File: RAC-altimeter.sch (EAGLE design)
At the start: 16 parts, among them IC1 BMI088, IC2 BMP388, IC3 STM32L412KBU6, J1 MICRO-SD

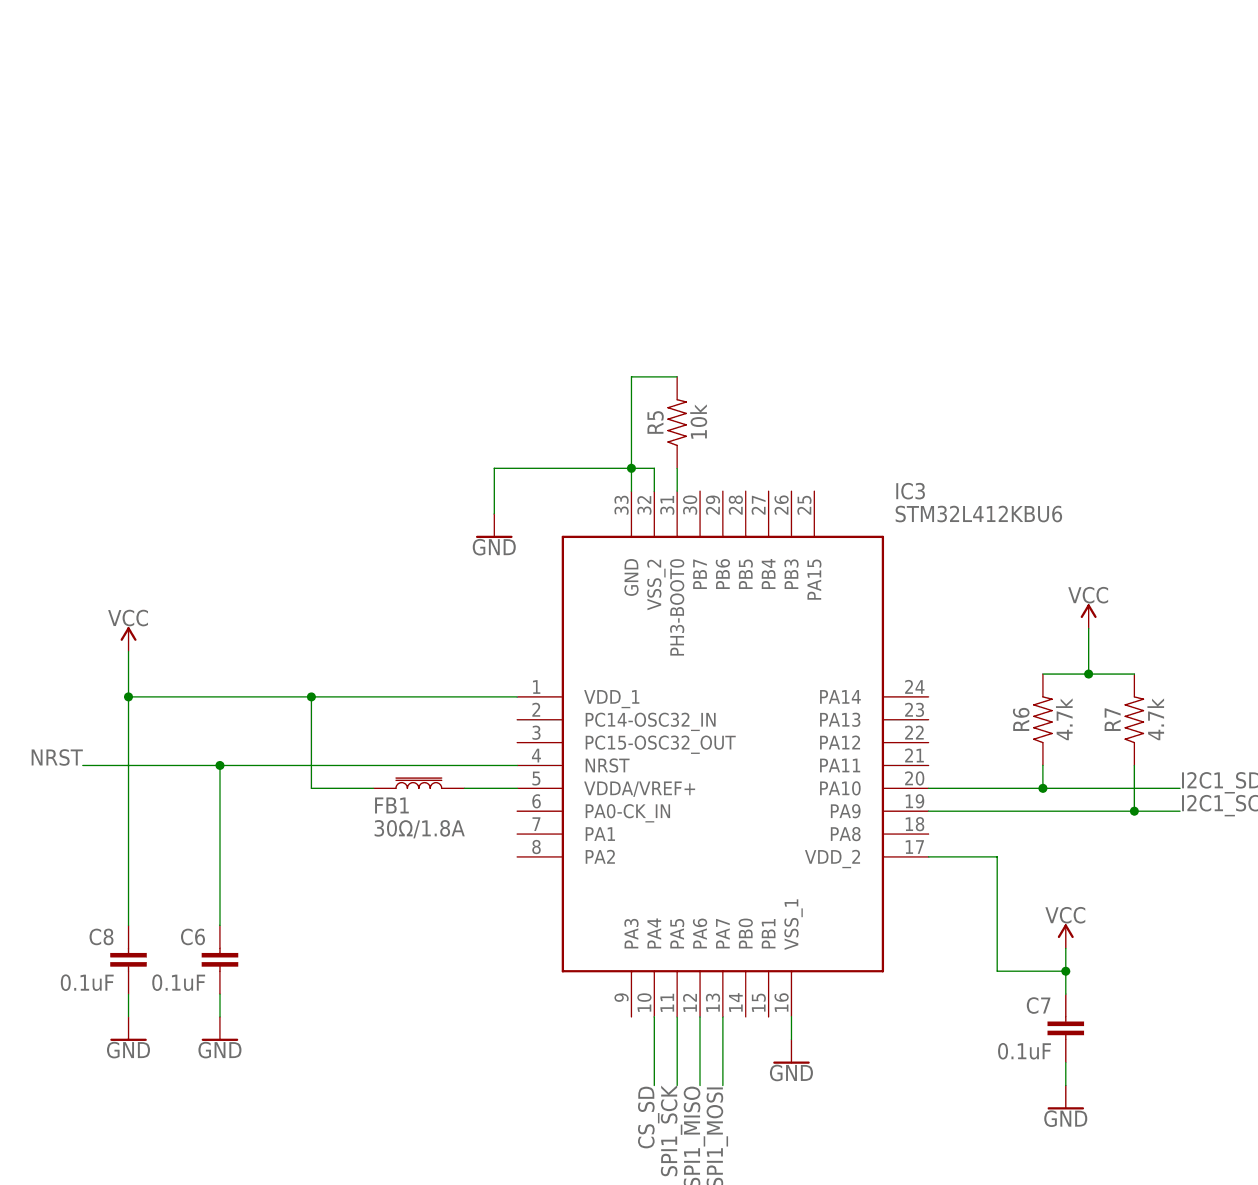
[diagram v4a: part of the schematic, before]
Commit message: Connected the TPS73733 LDO
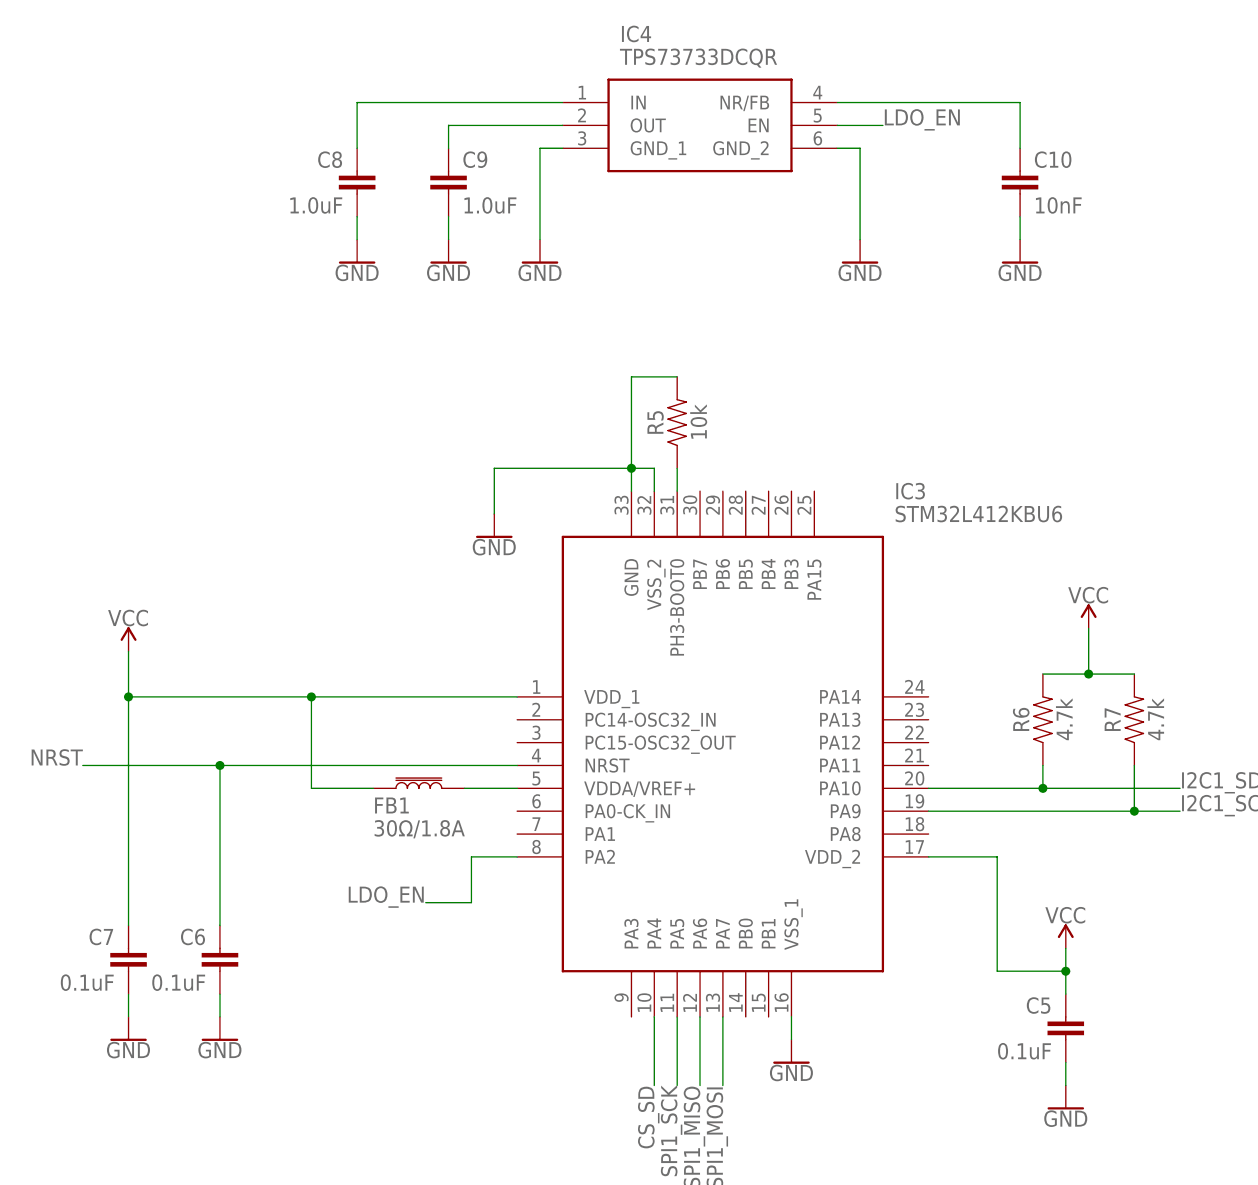
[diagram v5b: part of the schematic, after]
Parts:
- added C10: 10nF, SparkFun-Capacitors:10NF-0603-50V-10%
- added C5: 0.1uF, SparkFun-Capacitors:0.1UF-0603-25V-(+80/-20%)
- added C9: 1.0uF, SparkFun-Capacitors:1.0UF-0603-16V-10%
- added IC4: TPS73733DCQR, RAC-Altimeter:TPS73733DCQR
- C8: value 0.1uF -> 1.0uF; device SparkFun-Capacitors:0.1UF-0603-25V-(+80/-20%) -> SparkFun-Capacitors:1.0UF-0603-16V-10%
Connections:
- new net LDO_EN: IC3.PA2, IC4.EN
- new net N$1: C8.1, IC4.IN
- new net N$2: C9.1, IC4.OUT
- new net N$8: C10.1, IC4.NR/FB
- net GND: now also C10.2, C5.2, C9.2, IC4.GND_1, IC4.GND_2
- net VCC: now also C5.1; no longer C8.1
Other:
- moved on the sheet: C7, C8
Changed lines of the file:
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@@
 <?xml version="1.0" encoding="utf-8"?>
 <!DOCTYPE eagle SYSTEM "eagle.dtd">
-<eagle version="9.4.1">
+<eagle version="9.4.2">
 <drawing>
 <settings>
@@
 <part name="C6" library="SparkFun-Capacitors" deviceset="0.1UF" device="-0603-25V-(+80/-20%)" value="0.1uF"/>
 <part name="GND7" library="SparkFun-PowerSymbols" library_urn="urn:adsk.eagle:library:530" deviceset="GND" device=""/>
+<part name="C5" library="SparkFun-Capacitors" deviceset="0.1UF" device="-0603-25V-(+80/-20%)" value="0.1uF"/>
+<part name="GND8" library="SparkFun-PowerSymbols" library_urn="urn:adsk.eagle:library:530" deviceset="GND" device=""/>
 <part name="C7" library="SparkFun-Capacitors" deviceset="0.1UF" device="-0603-25V-(+80/-20%)" value="0.1uF"/>
-<part name="GND8" library="SparkFun-PowerSymbols" library_urn="urn:adsk.eagle:library:530" deviceset="GND" device=""/>
-<part name="C8" library="SparkFun-Capacitors" deviceset="0.1UF" device="-0603-25V-(+80/-20%)" value="0.1uF"/>
 <part name="GND9" library="SparkFun-PowerSymbols" library_urn="urn:adsk.eagle:library:530" deviceset="GND" device=""/>
 <part name="GND10" library="SparkFun-PowerSymbols" library_urn="urn:adsk.eagle:library:530" deviceset="GND" device=""/>
@@
 <part name="C4" library="SparkFun-Capacitors" deviceset="0.1UF" device="-0603-25V-(+80/-20%)" value="0.1uF"/>
 <part name="GND5" library="SparkFun-PowerSymbols" library_urn="urn:adsk.eagle:library:530" deviceset="GND" device=""/>
+<part name="IC4" library="RAC-Altimeter" deviceset="TPS73733DCQR" device=""/>
+<part name="C8" library="SparkFun-Capacitors" deviceset="1.0UF" device="-0603-16V-10%" value="1.0uF"/>
+<part name="C9" library="SparkFun-Capacitors" deviceset="1.0UF" device="-0603-16V-10%" value="1.0uF"/>
+<part name="GND6" library="SparkFun-PowerSymbols" library_urn="urn:adsk.eagle:library:530" deviceset="GND" device=""/>
+<part name="GND12" library="SparkFun-PowerSymbols" library_urn="urn:adsk.eagle:library:530" deviceset="GND" device=""/>
+<part name="GND13" library="SparkFun-PowerSymbols" library_urn="urn:adsk.eagle:library:530" deviceset="GND" device=""/>
+<part name="GND14" library="SparkFun-PowerSymbols" library_urn="urn:adsk.eagle:library:530" deviceset="GND" device=""/>
+<part name="C10" library="SparkFun-Capacitors" deviceset="10NF" device="-0603-50V-10%" value="10nF"/>
+<part name="GND15" library="SparkFun-PowerSymbols" library_urn="urn:adsk.eagle:library:530" deviceset="GND" device=""/>
 </parts>
 <sheets>
@@
 <attribute name="VALUE" x="-27.94" y="20.066" size="1.778" layer="96" align="top-center"/>
 </instance>
-<instance part="C7" gate="G$1" x="66.04" y="20.32" smashed="yes" rot="MR0">
+<instance part="C5" gate="G$1" x="66.04" y="20.32" smashed="yes" rot="MR0">
 <attribute name="NAME" x="64.516" y="23.241" size="1.778" layer="95" font="vector" rot="MR0"/>
 <attribute name="VALUE" x="64.516" y="18.161" size="1.778" layer="96" font="vector" rot="MR0"/>
@@
 <attribute name="VALUE" x="66.04" y="12.446" size="1.778" layer="96" align="top-center"/>
 </instance>
-<instance part="C8" gate="G$1" x="-38.1" y="27.94" smashed="yes" rot="MR0">
+<instance part="C7" gate="G$1" x="-38.1" y="27.94" smashed="yes" rot="MR0">
 <attribute name="NAME" x="-39.624" y="30.861" size="1.778" layer="95" font="vector" rot="MR0"/>
 <attribute name="VALUE" x="-39.624" y="25.781" size="1.778" layer="96" font="vector" rot="MR0"/>
@@
 <instance part="GND5" gate="1" x="180.34" y="99.06" smashed="yes">
 <attribute name="VALUE" x="180.34" y="98.806" size="1.778" layer="96" align="top-center"/>
+</instance>
+<instance part="IC4" gate="G$1" x="10.16" y="124.46" smashed="yes">
+<attribute name="NAME" x="16.51" y="132.08" size="1.778" layer="95" align="center-left"/>
+<attribute name="VALUE" x="16.51" y="129.54" size="1.778" layer="96" align="center-left"/>
+</instance>
+<instance part="C8" gate="G$1" x="-12.7" y="114.3" smashed="yes" rot="MR0">
+<attribute name="NAME" x="-14.224" y="117.221" size="1.778" layer="95" font="vector" rot="MR0"/>
+<attribute name="VALUE" x="-14.224" y="112.141" size="1.778" layer="96" font="vector" rot="MR0"/>
+</instance>
+<instance part="C9" gate="G$1" x="-2.54" y="114.3" smashed="yes">
+<attribute name="NAME" x="-1.016" y="117.221" size="1.778" layer="95" font="vector"/>
+<attribute name="VALUE" x="-1.016" y="112.141" size="1.778" layer="96" font="vector"/>
+</instance>
+<instance part="GND6" gate="1" x="-2.54" y="106.68" smashed="yes">
+<attribute name="VALUE" x="-2.54" y="106.426" size="1.778" layer="96" align="top-center"/>
+</instance>
+<instance part="GND12" gate="1" x="-12.7" y="106.68" smashed="yes">
+<attribute name="VALUE" x="-12.7" y="106.426" size="1.778" layer="96" align="top-center"/>
+</instance>
+<instance part="GND13" gate="1" x="43.18" y="106.68" smashed="yes">
+<attribute name="VALUE" x="43.18" y="106.426" size="1.778" layer="96" align="top-center"/>
+</instance>
+<instance part="GND14" gate="1" x="7.62" y="106.68" smashed="yes">
+<attribute name="VALUE" x="7.62" y="106.426" size="1.778" layer="96" align="top-center"/>
+</instance>
+<instance part="C10" gate="G$1" x="60.96" y="114.3" smashed="yes">
+<attribute name="NAME" x="62.484" y="117.221" size="1.778" layer="95" font="vector"/>
+<attribute name="VALUE" x="62.484" y="112.141" size="1.778" layer="96" font="vector"/>
+</instance>
+<instance part="GND15" gate="1" x="60.96" y="106.68" smashed="yes">
+<attribute name="VALUE" x="60.96" y="106.426" size="1.778" layer="96" align="top-center"/>
 </instance>
 </instances>
@@
 </segment>
 <segment>
-<pinref part="C7" gate="G$1" pin="2"/>
+<pinref part="C5" gate="G$1" pin="2"/>
 <pinref part="GND8" gate="1" pin="GND"/>
 <wire x1="66.04" y1="17.78" x2="66.04" y2="15.24" width="0.1524" layer="91"/>
 </segment>
 <segment>
-<pinref part="C8" gate="G$1" pin="2"/>
+<pinref part="C7" gate="G$1" pin="2"/>
 <pinref part="GND9" gate="1" pin="GND"/>
 <wire x1="-38.1" y1="22.86" x2="-38.1" y2="25.4" width="0.1524" layer="91"/>
@@
 <junction x="180.34" y="106.68"/>
 </segment>
+<segment>
+<pinref part="C8" gate="G$1" pin="2"/>
+<pinref part="GND12" gate="1" pin="GND"/>
+<wire x1="-12.7" y1="111.76" x2="-12.7" y2="109.22" width="0.1524" layer="91"/>
+</segment>
+<segment>
+<pinref part="C9" gate="G$1" pin="2"/>
+<pinref part="GND6" gate="1" pin="GND"/>
+<wire x1="-2.54" y1="111.76" x2="-2.54" y2="109.22" width="0.1524" layer="91"/>
+</segment>
+<segment>
+<pinref part="IC4" gate="G$1" pin="GND_2"/>
+<wire x1="40.64" y1="119.38" x2="43.18" y2="119.38" width="0.1524" layer="91"/>
+<pinref part="GND13" gate="1" pin="GND"/>
+<wire x1="43.18" y1="119.38" x2="43.18" y2="109.22" width="0.1524" layer="91"/>
+</segment>
+<segment>
+<pinref part="IC4" gate="G$1" pin="GND_1"/>
+<wire x1="10.16" y1="119.38" x2="7.62" y2="119.38" width="0.1524" layer="91"/>
+<pinref part="GND14" gate="1" pin="GND"/>
+<wire x1="7.62" y1="119.38" x2="7.62" y2="109.22" width="0.1524" layer="91"/>
+</segment>
+<segment>
+<pinref part="C10" gate="G$1" pin="2"/>
+<pinref part="GND15" gate="1" pin="GND"/>
+<wire x1="60.96" y1="111.76" x2="60.96" y2="109.22" width="0.1524" layer="91"/>
+</segment>
 </net>
 <net name="I2C1_SCL" class="0">
@@
 <pinref part="IC3" gate="G$1" pin="VDD_1"/>
 <wire x1="5.08" y1="58.42" x2="-17.78" y2="58.42" width="0.1524" layer="91"/>
-<pinref part="C8" gate="G$1" pin="1"/>
+<pinref part="C7" gate="G$1" pin="1"/>
 <wire x1="-17.78" y1="58.42" x2="-38.1" y2="58.42" width="0.1524" layer="91"/>
 <wire x1="-38.1" y1="58.42" x2="-38.1" y2="33.02" width="0.1524" layer="91"/>
@@
 </segment>
 <segment>
-<pinref part="C7" gate="G$1" pin="1"/>
+<pinref part="C5" gate="G$1" pin="1"/>
 <pinref part="SUPPLY5" gate="G$1" pin="VCC"/>
 <wire x1="66.04" y1="25.4" x2="66.04" y2="27.94" width="0.1524" layer="91"/>
@@
 </segment>
 </net>
+<net name="N$1" class="0">
+<segment>
+<pinref part="IC4" gate="G$1" pin="IN"/>
+<pinref part="C8" gate="G$1" pin="1"/>
+<wire x1="10.16" y1="124.46" x2="-12.7" y2="124.46" width="0.1524" layer="91"/>
+<wire x1="-12.7" y1="124.46" x2="-12.7" y2="119.38" width="0.1524" layer="91"/>
+</segment>
+</net>
+<net name="N$2" class="0">
+<segment>
+<pinref part="C9" gate="G$1" pin="1"/>
+<wire x1="-2.54" y1="119.38" x2="-2.54" y2="121.92" width="0.1524" layer="91"/>
+<pinref part="IC4" gate="G$1" pin="OUT"/>
+<wire x1="-2.54" y1="121.92" x2="10.16" y2="121.92" width="0.1524" layer="91"/>
+</segment>
+</net>
+<net name="LDO_EN" class="0">
+<segment>
+<pinref part="IC4" gate="G$1" pin="EN"/>
+<wire x1="40.64" y1="121.92" x2="45.72" y2="121.92" width="0.1524" layer="91"/>
+<label x="45.72" y="121.92" size="1.778" layer="95"/>
+</segment>
+<segment>
+<pinref part="IC3" gate="G$1" pin="PA2"/>
+<wire x1="5.08" y1="40.64" x2="0" y2="40.64" width="0.1524" layer="91"/>
+<wire x1="0" y1="40.64" x2="0" y2="35.56" width="0.1524" layer="91"/>
+<wire x1="0" y1="35.56" x2="-5.08" y2="35.56" width="0.1524" layer="91"/>
+<label x="-5.08" y="35.56" size="1.778" layer="95" rot="MR0"/>
+</segment>
+</net>
+<net name="N$8" class="0">
+<segment>
+<pinref part="IC4" gate="G$1" pin="NR/FB"/>
+<wire x1="40.64" y1="124.46" x2="60.96" y2="124.46" width="0.1524" layer="91"/>
+<pinref part="C10" gate="G$1" pin="1"/>
+<wire x1="60.96" y1="124.46" x2="60.96" y2="119.38" width="0.1524" layer="91"/>
+</segment>
+</net>
